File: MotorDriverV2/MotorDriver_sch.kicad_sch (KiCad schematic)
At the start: 16 parts, among them J5 Out_A, J6 Out_B, J8 Out_A, J9 Out_B, U1 DRV8871DDA, U2 DRV8871DDA

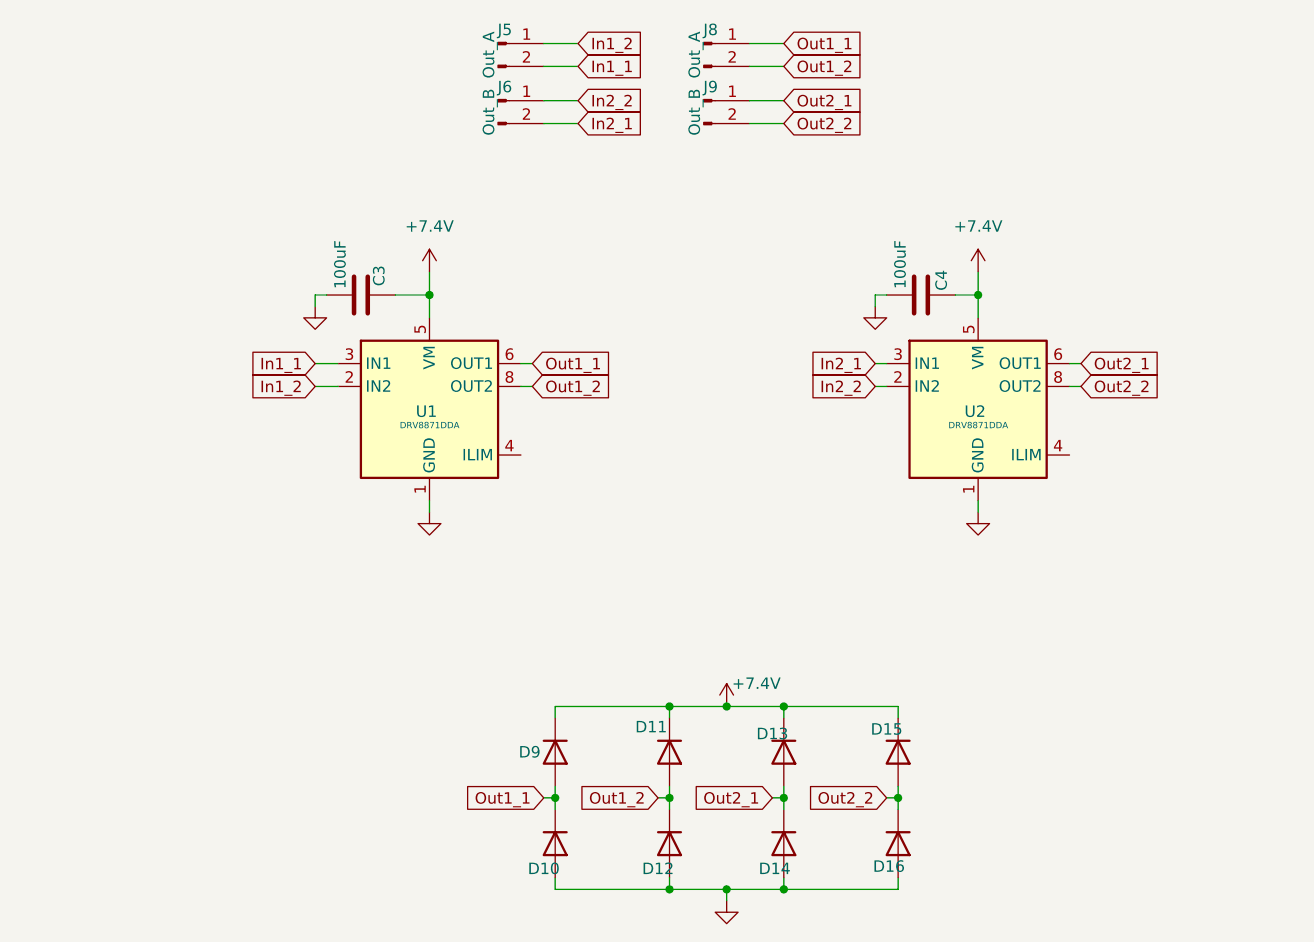
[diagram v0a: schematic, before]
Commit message: UPDATE: Added symbols, fotprints and datasheets for components
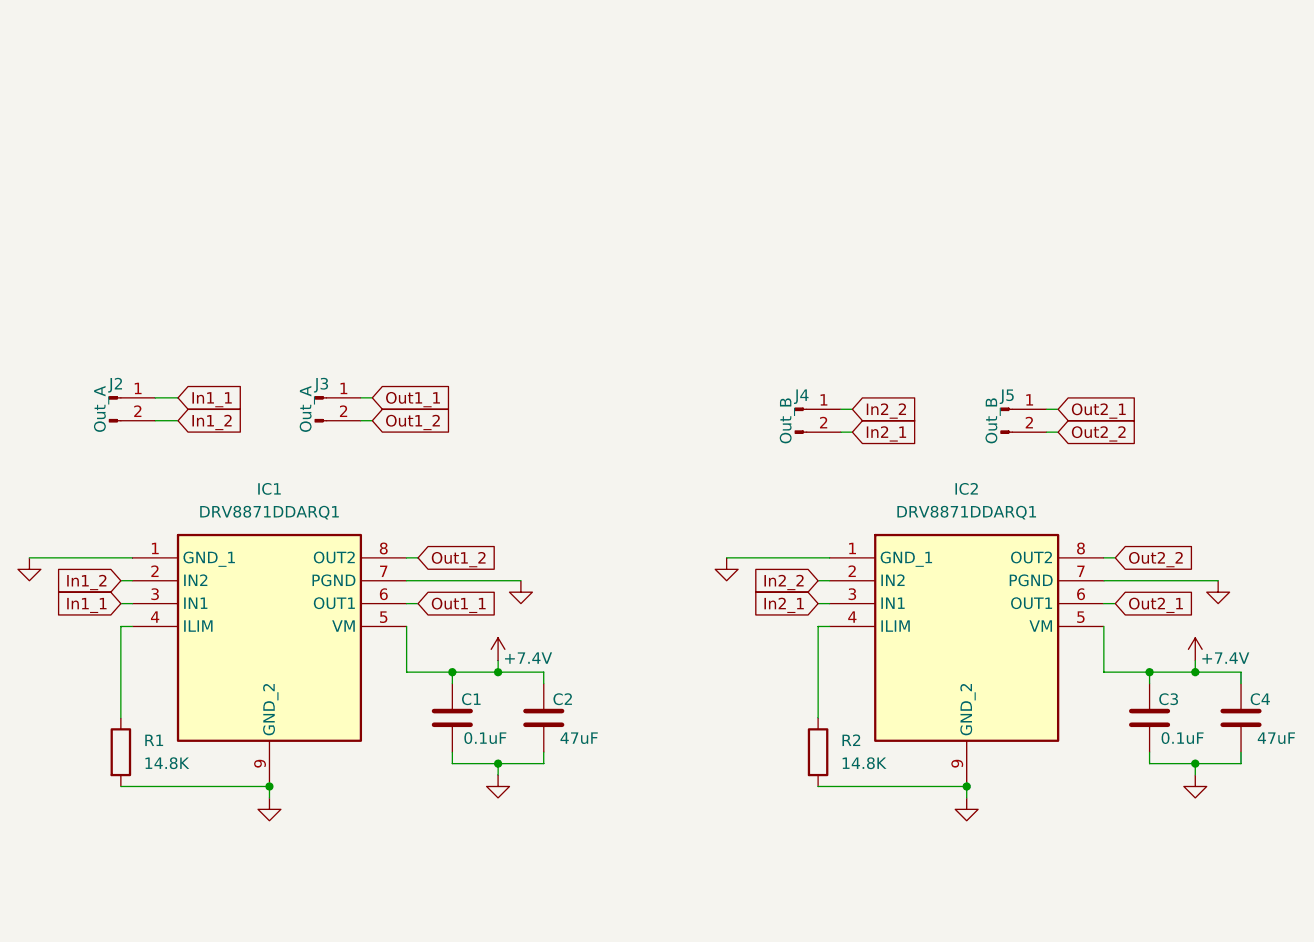
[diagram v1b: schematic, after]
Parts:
- removed D10, D11, D12, D13, D14, D15, D16, D9: 1N4001, Diode_THT:D_DO-41_SOD81_P10.16mm_Horizontal, symbol Diode:1N4001
- removed U1, U2: DRV8871DDA, Package_SO:Texas_HTSOP-8-1EP_3.9x4.9mm_P1.27mm_EP2.95x4.9mm_Mask2.4x3.1mm_ThermalVias, symbol Driver_Motor:DRV8871DDA
- added C1, C3: 0.1uF, Capacitor_SMD:C_0805_2012Metric_Pad1.18x1.45mm_HandSolder, symbol Device:C
- added IC1, IC2: DRV8871DDARQ1, DRV8871DDARQ1:SOIC127P600X170-9N, symbol DRV8871DDARQ1:DRV8871DDARQ1
- added R1, R2: 14.8K, Resistor_THT:R_Axial_DIN0207_L6.3mm_D2.5mm_P7.62mm_Horizontal, symbol Device:R
- C2: renamed from C3; value 100uF -> 47uF
- C4: value 100uF -> 47uF
- renumbered J5 to J2, J8 to J3, J6 to J4, J9 to J5
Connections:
- net +7.4V: now also C1.1, C3.1, IC1.5 (VM), IC2.5 (VM)
- net GND: now also C1.2, C3.2, IC1.1 (GND_1), IC1.7 (PGND), IC1.9 (GND_2), IC2.1 (GND_1), IC2.7 (PGND), IC2.9 (GND_2), R1.2, R2.2
- net In1_1: now also J2.1 (Pin_1), IC1.3 (IN1); no longer J2.2 (Pin_2)
- net In1_2: now also J2.2 (Pin_2), IC1.2 (IN2); no longer J2.1 (Pin_1)
- net In2_1: now also IC2.3 (IN1)
- net In2_2: now also IC2.2 (IN2)
- net Out1_1: now also IC1.6 (OUT1)
- net Out1_2: now also IC1.8 (OUT2)
- net Out2_1: now also IC2.6 (OUT1)
- net Out2_2: now also IC2.8 (OUT2)
- new net: IC1.4 (ILIM), R1.1
- new net: IC2.4 (ILIM), R2.1
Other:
- moved on the sheet: C2, J2, J3, J4, J5
